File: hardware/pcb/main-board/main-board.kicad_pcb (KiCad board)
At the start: 2 copper layers, 100 x 80 mm, 48 parts, among them J1 USB-C, J10 CH552G_KEYBOARD_MCU, J11 KEYBOARD_BACKLIGHT_LEDS, J12 SPEAKER_1W_8OHM, J2 BATT_2x18650_PARALLEL, J3 BOOT0_OVERRIDE_JUMPER, J4 SWD_DEBUG, J5 MICROSD, J6 CR2032_HOLDER, J7 U.FL, J8 SMA_EDGE, J9 RA8875_DISPLAY_MODULE, Q1 2N7002, SW1 PWR_KEY, SW2 RESET, U1 MCP73831-2-OT, U10 PAM8403D, U2 IP5306, U3 AMS1117-3.3, U4 AMS1117-3.3, U5 GD32VF103CCT6, U6 W25Q64JVSSIQ, U7 23LC1024, U8 DS3231M, U9 ESP32-C3-MINI-1U, Y1 8MHz

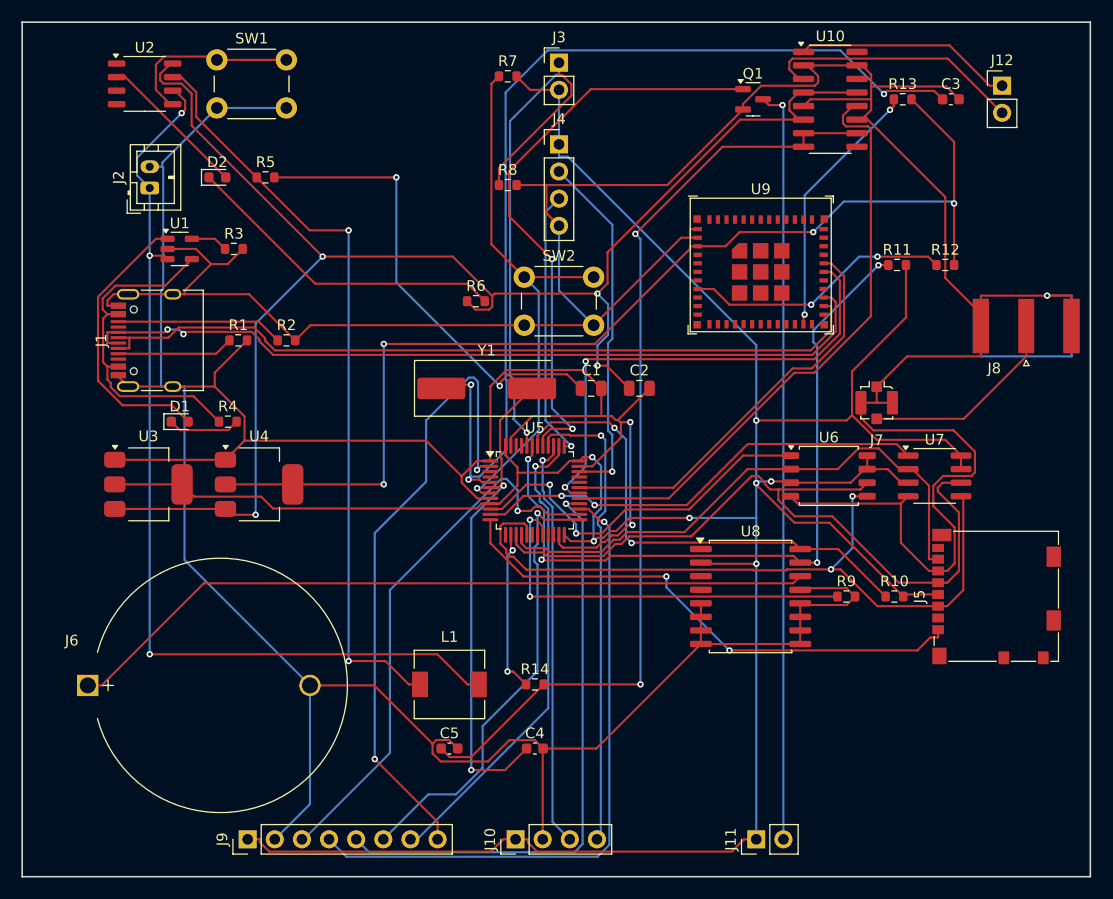
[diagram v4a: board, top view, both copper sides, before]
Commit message: hardware: ground the ESP32-C3-MINI-1U's remaining GND/thermal pads
The real footprint swapped in last commit has ~22 GND pin numbers
(30 physical pads once the pin-49 thermal array's 9 copper islands
are counted), but the schematic symbol only drew and wired 2 of them
-- flagged as a follow-up rather than fixed at the time.

Fixed: kicad_gen/build_library.py's ESP32-C3-MINI-1U symbol now draws
every real GND pin from the datasheet's Table 3-1 (1, 2, 11, 14,
36-53), wired to GND in build_schematic.py. Only the module's 14
genuinely NC pads stay undrawn -- there's nothing to connect them to.
Espressif's hardware design guidelines recommend grounding all GND
pads (not just a couple) for this module's RF and thermal performance.

Regenerated schematic (ERC clean) and PCB from scratch: fresh
placement, fresh Freerouting pass. Result: all 192 nets auto-routed
with nothing left to finish by hand -- the first PCB regeneration in
this board's history where Freerouting didn't get stuck on anything.
0 DRC violations, 0 unconnected items, all 30 of U9's GND pads
confirmed on the GND net.

Not done here: an actual copper ground pour/zone stitched to the
thermal pad via array. The pads are now electrically grounded via
ordinary routed traces, which satisfies connectivity but not the full
thermal-performance intent of Espressif's guidance -- left as a
separate PCB-editor task.

Co-Authored-By: Claude Sonnet 5 <noreply@anthropic.com>
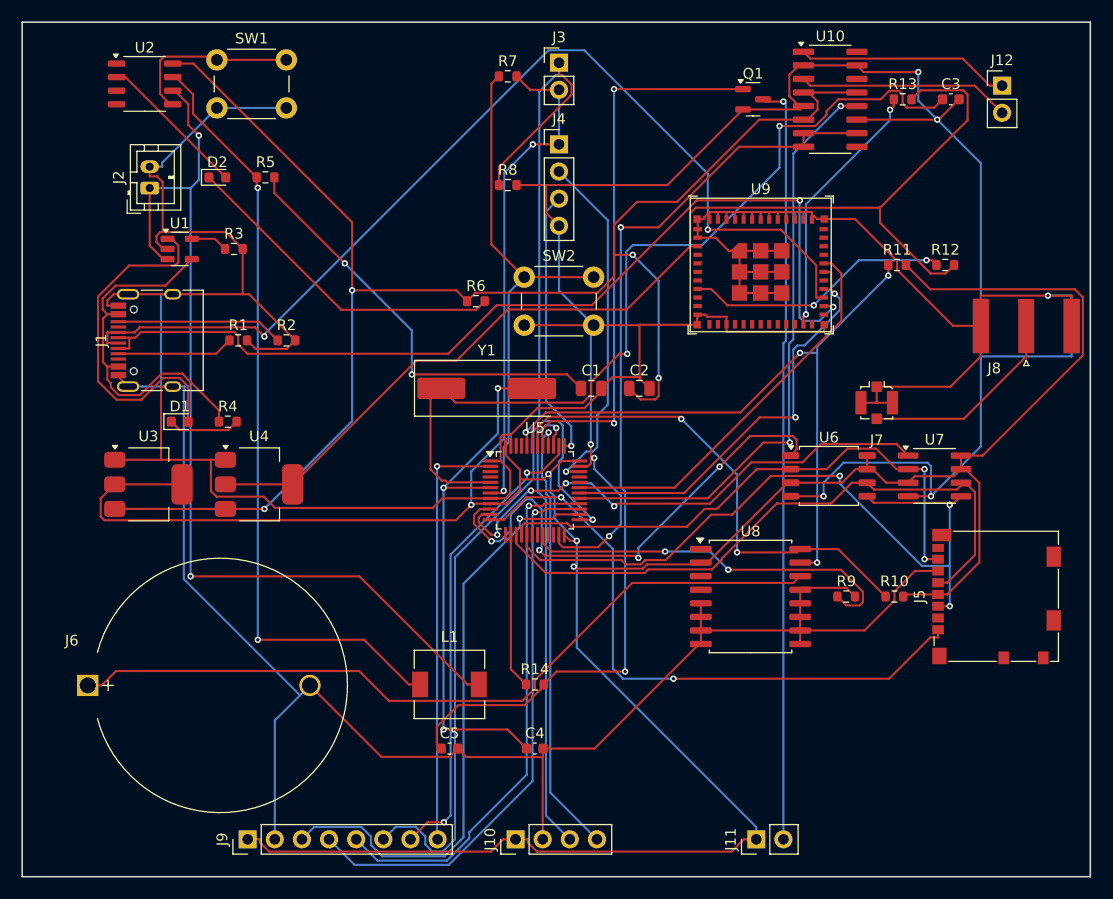
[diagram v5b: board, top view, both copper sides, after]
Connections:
- U9 pad 11: (no net) -> GND
- U9 pad 14: (no net) -> GND
- U9 pad 36: (no net) -> GND
- U9 pad 37: (no net) -> GND
- U9 pad 38: (no net) -> GND
- U9 pad 39: (no net) -> GND
- U9 pad 40: (no net) -> GND
- U9 pad 41: (no net) -> GND
- U9 pad 42: (no net) -> GND
- U9 pad 43: (no net) -> GND
- U9 pad 44: (no net) -> GND
- U9 pad 45: (no net) -> GND
- U9 pad 46: (no net) -> GND
- U9 pad 47: (no net) -> GND
- U9 pad 48: (no net) -> GND
- U9 pad 49: (no net) -> GND
- U9 pad 50: (no net) -> GND
- U9 pad 51: (no net) -> GND
- U9 pad 52: (no net) -> GND
- U9 pad 53: (no net) -> GND
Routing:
- net GND: track 576.5 -> 609.5 mm, vias 3 -> 8
- net /DISP_CS: track 42.5 -> 65.2 mm
- net /DISP_INT: track 60.0 -> 39.9 mm, vias 2 -> 1
- net /USB_DP: track 76.5 -> 95.3 mm
- net /USB_DN: track 73.9 -> 89.1 mm, vias 0 -> 2
- net /FLASH_CS: track 35.2 -> 47.9 mm, vias 2 -> 4
- net /OSC_IN: track 96.6 -> 84.0 mm, vias 3 -> 2
- net /SPI1_SCK: track 70.7 -> 59.8 mm
- net /+3V3_MCU: track 293.4 -> 303.9 mm, vias 7 -> 5
- net /SD_CS: track 50.1 -> 58.7 mm
- net /SPI2_MISO: track 60.6 -> 52.8 mm
- net /CHG_STAT: track 26.6 -> 33.2 mm
- net /SRAM_CS: track 43.0 -> 48.8 mm, vias 2 -> 4
- net /USART1_TX: track 45.9 -> 40.1 mm
- net /I2C1_SDA: track 69.3 -> 63.6 mm, vias 4 -> 3
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
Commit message: hardware: pre-fab design review of the Main Board, REV 0.7
Ran the design-review pass the Project Status table has been calling the
next step. Four findings on the board and one on the tooling.

Reference-designator drift. build_schematic.py auto-numbered refdes by
call order while build_pcb.py's PLACEMENT dict is keyed by refdes, so
adding the IP5306's inductor and snubber (615f5d2) renumbered every
later R and C by +1 and silently built a dozen parts into each other's
board positions. Measured on the committed board: the 8MHz crystal's
20pF load caps were 51mm and 34mm from the crystal, the IP5306's 22uF
snubber and VOUT caps were ~50mm from the IC, the audio filter's R and C
were 61mm and 70mm from the amplifier. Crystal load caps that far from
their crystal do not work -- this was a dead board that looked fine.

Fixed on both sides: all 48 components now pass an explicit ref= and
schematic.py's place() refuses to place anything without one, so refdes
is a declaration rather than a side effect of file order; and PLACEMENT
entries carry the expected component value, checked against the netlist
before anything is placed. build_pcb.py also now fails on courtyard
overlaps and on PLACEMENT entries not present in the netlist.

The IP5306 switching loop. Independent of the drift above, the inductor
commit placed L1 63mm from U2 with the VOUT cap 68mm away, in the open
band below the MCU. A 1uH boost converter's SW-node loop area is set by
exactly that distance. L1, the RC snubber and the VOUT cap now sit tight
around U2, whose BAT/SW/VOUT pins are all on its right-hand side; SW1
moved to the MCU column to make room, being a momentary switch on a
static input.

Trace widths. Everything was routed at the 0.2mm default including the
2.4A boost path, flagged for review when the inductor was added.
Netclasses now live in main-board.kicad_pro, written by build_pcb.py
before the board goes to the autorouter: 0.8mm for /VBATT and
/IP5306_SW, 0.4mm for +5V and VBUS, sized per IP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
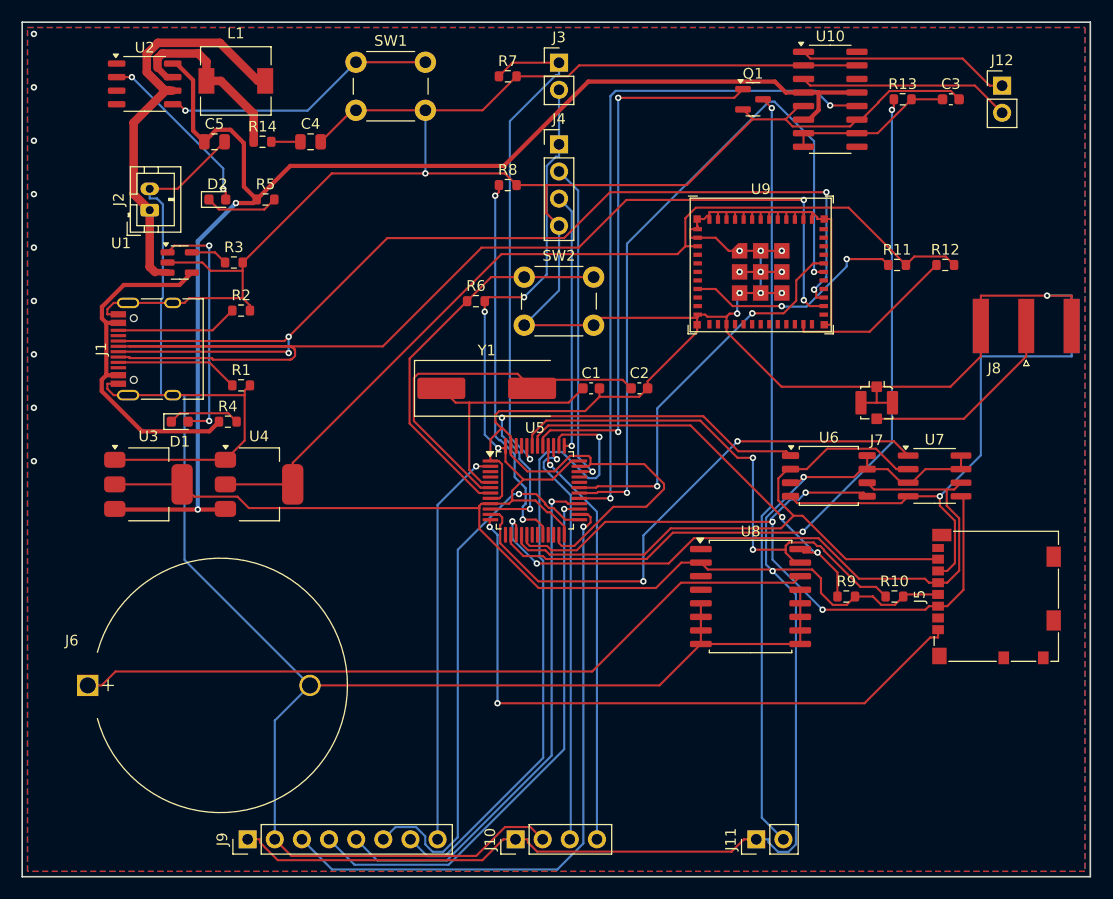
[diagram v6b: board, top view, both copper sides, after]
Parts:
- C1, C2: value 22uF -> 20pF; footprint C_0805_2012Metric -> C_0603_1608Metric
- C3: value 20pF -> 100nF
- C4: value 20pF -> 22uF; footprint C_0603_1608Metric -> C_0805_2012Metric
- C5: value 100nF -> 22uF; footprint C_0603_1608Metric -> C_0805_2012Metric
- R11: value 4.7k -> 10k
- R13: value 10k -> 1k
- R14: value 1k -> 0.5R
- R5: value 0.5R -> 1k
- R6: value 1k -> 10k
- R9: value 10k -> 4.7k
- moved C5 60.9 mm to (18.0, 11.2)
- moved C4 60.6 mm to (27.0, 11.2)
- moved L1 59.9 mm to (20.0, 5.50)
- moved R14 56.8 mm to (22.5, 11.2)
- moved SW1 13.0 mm to (31.2, 3.75)
- moved R2 5.08 mm to (20.5, 27.0)
- moved R1 4.22 mm to (20.5, 34.0)
- moved D2 2.07 mm to (18.3, 16.6)
- moved J2 2.07 mm to (11.9, 17.6)
- moved R5 2.07 mm to (22.8, 16.6)
- moved R3 1.27 mm to (19.8, 22.5)
- moved U1 1.27 mm to (14.8, 22.5)
- moved J1 0.81 mm to (13.1, 30.6)
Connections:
- C1 pad 1: /SNUBBER_MID -> /OSC_IN
- C2 pad 1: +5V -> /OSC_OUT
- C3 pad 1: /OSC_IN -> /AUDIO_IN
- C4 pad 1: /OSC_OUT -> /SNUBBER_MID
- C5 pad 1: /AUDIO_IN -> +5V
- R10 pad 1: /I2C1_SCL -> /I2C1_SDA
- R11 pad 1: /I2C1_SDA -> /ESP_EN
- R11 pad 2: /+3V3_MCU -> /+3V3_RF
- R12 pad 1: /ESP_EN -> /ESP_IO9
- R13 pad 1: /ESP_IO9 -> /AUDIO_PWM
- R13 pad 2: /+3V3_RF -> /AUDIO_IN
- R14 pad 1: /AUDIO_PWM -> /IP5306_SW
- R14 pad 2: /AUDIO_IN -> /SNUBBER_MID
- R5 pad 1: /IP5306_SW -> +5V
- R5 pad 2: /SNUBBER_MID -> /BATT_LED1_R
- R6 pad 1: +5V -> /NRST
- R6 pad 2: /BATT_LED1_R -> /+3V3_MCU
- R7 pad 1: /NRST -> /BOOT0
- R7 pad 2: /+3V3_MCU -> GND
- R8 pad 1: /BOOT0 -> /BOOT1
- R9 pad 1: /BOOT1 -> /I2C1_SCL
- R9 pad 2: GND -> /+3V3_MCU
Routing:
- net /AUDIO_IN: track 90.3 -> 15.6 mm, vias 2 -> 0
- net /OSC_IN: track 84.0 -> 23.1 mm, vias 2 -> 0
- net /AUDIO_PWM: track 14.6 -> 73.8 mm, vias 0 -> 2
- net /IP5306_SW: track 73.1 -> 17.9 mm, vias 2 -> 0
- net /VBATT: track 89.5 -> 38.5 mm, vias 2 -> 0
- net /+3V3_MCU: track 303.9 -> 261.2 mm
- net /SNUBBER_MID: track 40.2 -> 2.73 mm, vias 2 -> 0
- net /USART1_TX: track 40.1 -> 65.6 mm
- net /USB_DN: track 89.1 -> 114.4 mm
- net /BATT_LED1_R: track 31.3 -> 6.90 mm
- net GND: track 609.5 -> 632.1 mm, vias 8 -> 22
- net +5V: track 148.1 -> 126.5 mm, vias 4 -> 2
- net /+3V3_RF: track 104.9 -> 85.7 mm
- net /DISP_RESET: track 44.2 -> 60.3 mm, vias 2 -> 1
- net /OSC_OUT: track 50.2 -> 35.5 mm, vias 3 -> 0
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- added copper zone on B.Cu, net GND
- added copper zone on F.Cu, net GND

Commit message: hardware: remove the Main Board's antenna path, fix the stitching grid
This pass set out to do the item that headed the Main Board's "What's not
done yet": controlled-impedance layout for the 2.4GHz antenna path. There
is no antenna path. `/ANT_RF` has no `U9` pad on it -- the net was two
connectors wired to each other, with nothing driving them.

The ESP32-C3-MINI-1U does not bring its radio out to a castellated pad.
Datasheet v2.2 Table 3-1 lists all 53: pins 1, 2, 11, 14 and 36-53 are
GND, the rest are 3V3, EN and IO. The radio leaves through the antenna
jack mounted on the module -- that is what the "U" in -1U means. So:

- build_library.py's symbol carried a pin whose *number* was the string
  "ANT", matching no pad in the footprint. KiCad ties pins to pads by
  number, so a number matching nothing contributes nothing, and the
  netlist produced a two-connector net rather than an error.
- J7 was a second, board-mounted U.FL duplicating the module's own. The
  schematic comment beside it said as much ("U.FL pad on the
  ESP32-C3-MINI-1U module itself") and it was placed on the PCB anyway.
- The J7->J8 trace was therefore 19mm of 0.2mm copper between two
  connectors -- the net an RF review would have been asked to match.
- An edge-mount SMA cannot be reached by a pigtail in any case: its
  centre pin is a board pad. bom.md items 13 and 14 specified exactly
  that pair, which cannot be assembled as written.
- And the pigtail was the wrong connector generation. Section 10.2
  specifies the module's jack as the third generation -- Hirose W.FL,
  I-PEX MHF III, Amphenol AMC, body 2.05 x 1.7 x 1.40mm (Figure 10-3).
  U.FL / MHF I is the first generation, ~2.6mm, and does not mate.

J7, J8, /ANT_RF and the invented ANT pin are gone from the symbol, the
schematic, PLACEMENT and the board. The antenna is a cable assembly and a
case feature: MHF III pigtail from the module's own jack to a bulkhead
SMA in the enclosure wall. That closes the RF layout gap by removing it --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
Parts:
- removed J7: U.FL, U.FL_Molex_MCRF_73412-0110_Vertical
- removed J8: SMA_EDGE, SMA_Amphenol_132289_EdgeMount
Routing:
- net /ANT_RF: track 19.3 -> 0.00 mm
- net GND: vias 22 -> 180
